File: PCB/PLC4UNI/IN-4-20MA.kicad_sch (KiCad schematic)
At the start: 8 parts

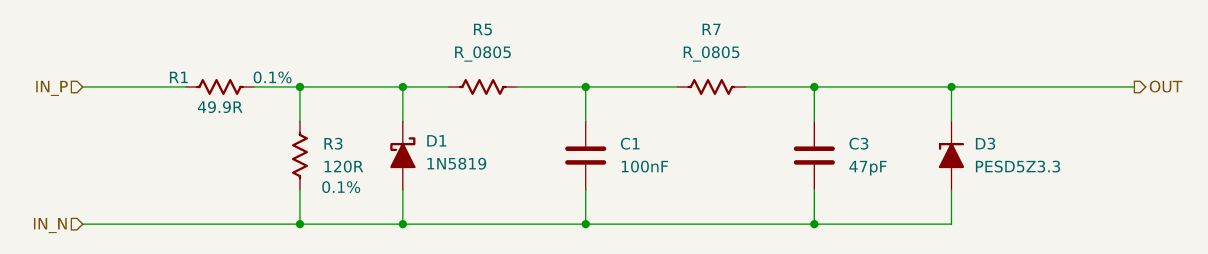
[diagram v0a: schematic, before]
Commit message: add ruteo buck-converter, inputs pnp,npn
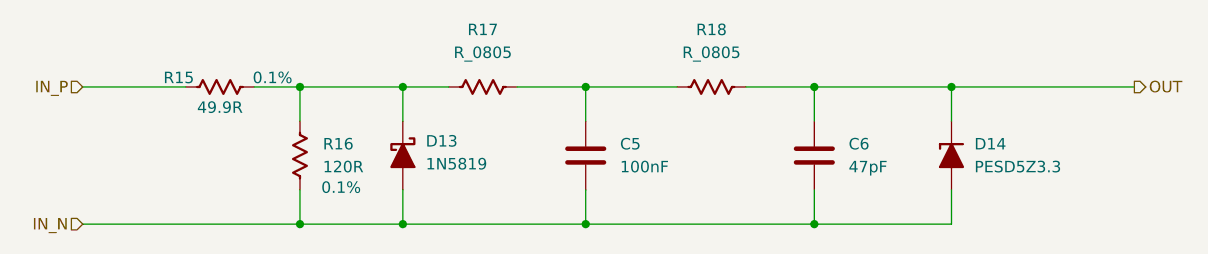
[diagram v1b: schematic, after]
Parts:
- renumbered C1 to C5, C3 to C6, D1 to D13, D3 to D14, R1 to R15, R3 to R16, R5 to R17, R7 to R18
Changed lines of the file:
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@@
 		(dnp no)
 		(fields_autoplaced yes)
-		(property "Reference" "R7"
+		(property "Reference" "R18"
 			(at 144.78 43.18 90)
 			(show_name no)
@@
 			(project "PLC4UNI"
 				(path "/f171b770-6a1a-4d3a-9dbb-25a622b94557/79ee6e1c-834c-43ff-8dcc-1385cc20b4c2/a71cebd4-7657-453a-a956-fcb918a861e5"
-					(reference "R7")
+					(reference "R18")
 					(unit 1)
 				)
 				(path "/f171b770-6a1a-4d3a-9dbb-25a622b94557/79ee6e1c-834c-43ff-8dcc-1385cc20b4c2/cfa02fc3-9ab3-4d43-96df-3d846bf37da2"
-					(reference "R8")
+					(reference "R22")
 					(unit 1)
 				)
@@
 		(in_pos_files yes)
 		(dnp no)
-		(property "Reference" "R3"
+		(property "Reference" "R16"
 			(at 101.6 55.8799 0)
 			(show_name no)
@@
 			(project "PLC4UNI"
 				(path "/f171b770-6a1a-4d3a-9dbb-25a622b94557/79ee6e1c-834c-43ff-8dcc-1385cc20b4c2/a71cebd4-7657-453a-a956-fcb918a861e5"
-					(reference "R3")
+					(reference "R16")
 					(unit 1)
 				)
 				(path "/f171b770-6a1a-4d3a-9dbb-25a622b94557/79ee6e1c-834c-43ff-8dcc-1385cc20b4c2/cfa02fc3-9ab3-4d43-96df-3d846bf37da2"
-					(reference "R4")
+					(reference "R20")
 					(unit 1)
 				)
@@
 		(dnp no)
 		(fields_autoplaced yes)
-		(property "Reference" "D1"
+		(property "Reference" "D13"
 			(at 113.03 55.5624 90)
 			(show_name no)
@@
 			(project "PLC4UNI"
 				(path "/f171b770-6a1a-4d3a-9dbb-25a622b94557/79ee6e1c-834c-43ff-8dcc-1385cc20b4c2/a71cebd4-7657-453a-a956-fcb918a861e5"
-					(reference "D1")
+					(reference "D13")
 					(unit 1)
 				)
 				(path "/f171b770-6a1a-4d3a-9dbb-25a622b94557/79ee6e1c-834c-43ff-8dcc-1385cc20b4c2/cfa02fc3-9ab3-4d43-96df-3d846bf37da2"
-					(reference "D2")
+					(reference "D15")
 					(unit 1)
 				)
@@
 		(dnp no)
 		(fields_autoplaced yes)
-		(property "Reference" "C3"
+		(property "Reference" "C6"
 			(at 160.02 55.8799 0)
 			(show_name no)
@@
 			(project "PLC4UNI"
 				(path "/f171b770-6a1a-4d3a-9dbb-25a622b94557/79ee6e1c-834c-43ff-8dcc-1385cc20b4c2/a71cebd4-7657-453a-a956-fcb918a861e5"
-					(reference "C3")
+					(reference "C6")
 					(unit 1)
 				)
 				(path "/f171b770-6a1a-4d3a-9dbb-25a622b94557/79ee6e1c-834c-43ff-8dcc-1385cc20b4c2/cfa02fc3-9ab3-4d43-96df-3d846bf37da2"
-					(reference "C4")
+					(reference "C8")
 					(unit 1)
 				)
@@
 		(dnp no)
 		(fields_autoplaced yes)
-		(property "Reference" "R5"
+		(property "Reference" "R17"
 			(at 119.38 43.18 90)
 			(show_name no)
@@
 			(project "PLC4UNI"
 				(path "/f171b770-6a1a-4d3a-9dbb-25a622b94557/79ee6e1c-834c-43ff-8dcc-1385cc20b4c2/a71cebd4-7657-453a-a956-fcb918a861e5"
-					(reference "R5")
+					(reference "R17")
 					(unit 1)
 				)
 				(path "/f171b770-6a1a-4d3a-9dbb-25a622b94557/79ee6e1c-834c-43ff-8dcc-1385cc20b4c2/cfa02fc3-9ab3-4d43-96df-3d846bf37da2"
-					(reference "R6")
+					(reference "R21")
 					(unit 1)
 				)
@@
 		(in_pos_files yes)
 		(dnp no)
-		(property "Reference" "R1"
+		(property "Reference" "R15"
 			(at 85.598 48.514 90)
 			(show_name no)
@@
 			(project "PLC4UNI"
 				(path "/f171b770-6a1a-4d3a-9dbb-25a622b94557/79ee6e1c-834c-43ff-8dcc-1385cc20b4c2/a71cebd4-7657-453a-a956-fcb918a861e5"
-					(reference "R1")
+					(reference "R15")
 					(unit 1)
 				)
 				(path "/f171b770-6a1a-4d3a-9dbb-25a622b94557/79ee6e1c-834c-43ff-8dcc-1385cc20b4c2/cfa02fc3-9ab3-4d43-96df-3d846bf37da2"
-					(reference "R2")
+					(reference "R19")
 					(unit 1)
 				)
@@
 		(dnp no)
 		(fields_autoplaced yes)
-		(property "Reference" "C1"
+		(property "Reference" "C5"
 			(at 134.62 55.8799 0)
 			(show_name no)
@@
 			(project "PLC4UNI"
 				(path "/f171b770-6a1a-4d3a-9dbb-25a622b94557/79ee6e1c-834c-43ff-8dcc-1385cc20b4c2/a71cebd4-7657-453a-a956-fcb918a861e5"
-					(reference "C1")
+					(reference "C5")
 					(unit 1)
 				)
 				(path "/f171b770-6a1a-4d3a-9dbb-25a622b94557/79ee6e1c-834c-43ff-8dcc-1385cc20b4c2/cfa02fc3-9ab3-4d43-96df-3d846bf37da2"
-					(reference "C2")
+					(reference "C7")
 					(unit 1)
 				)
@@
 		(dnp no)
 		(fields_autoplaced yes)
-		(property "Reference" "D3"
+		(property "Reference" "D14"
 			(at 173.99 55.8799 90)
 			(show_name no)
@@
 			(project "PLC4UNI"
 				(path "/f171b770-6a1a-4d3a-9dbb-25a622b94557/79ee6e1c-834c-43ff-8dcc-1385cc20b4c2/a71cebd4-7657-453a-a956-fcb918a861e5"
-					(reference "D3")
+					(reference "D14")
 					(unit 1)
 				)
 				(path "/f171b770-6a1a-4d3a-9dbb-25a622b94557/79ee6e1c-834c-43ff-8dcc-1385cc20b4c2/cfa02fc3-9ab3-4d43-96df-3d846bf37da2"
-					(reference "D4")
-					(unit 1)
-				)
+					(reference "D16")
+					(unit 1)
+				)

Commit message: 0-10V input, 4-20mA input
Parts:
- removed D13: 1N5819, PCM_Diode_THT_AKL:D_DO-41_SOD81_P7.62mm_Horizontal, symbol PCM_Diode_Schottky_AKL:1N5819
- added D13: 1N5819HW-7-F, EasyEDA:SOD-123_L2.7-W1.6-LS3.7-RD, symbol EasyEDA:1N5819HW-7-F
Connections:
- net IN_N: now also D13.2
- net at R15.2, R16.2, R17.1: now also D13.1
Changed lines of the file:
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@@
 	(wire
 		(pts
-			(xy 110.49 49.53) (xy 110.49 53.34)
+			(xy 110.49 49.53) (xy 110.49 52.07)
 		)
 		(stroke
@@
 	(wire
 		(pts
-			(xy 110.49 60.96) (xy 110.49 64.77)
-		)
-		(stroke
-			(width 0)
-			(type default)
-		)
-	)
-	(wire
-		(pts
 			(xy 123.19 49.53) (xy 130.81 49.53)
 		)
@@
 		(pts
 			(xy 171.45 49.53) (xy 171.45 53.34)
+		)
+		(stroke
+			(width 0)
+			(type default)
+		)
+	)
+	(wire
+		(pts
+			(xy 110.49 62.23) (xy 110.49 64.77)
 		)
 		(stroke
@@
 	)
 	(symbol
-		(lib_id "PCM_Diode_Schottky_AKL:1N5819")
-		(at 110.49 57.15 90)
-		(unit 1)
-		(body_style 1)
-		(exclude_from_sim no)
-		(in_bom yes)
-		(on_board yes)
-		(in_pos_files yes)
-		(dnp no)
-		(fields_autoplaced yes)
-		(property "Reference" "D13"
-			(at 113.03 55.5624 90)
-			(show_name no)
-			(do_not_autoplace no)
-			(effects
-				(font
-					(size 1.27 1.27)
-				)
-				(justify right)
-			)
-		)
-		(property "Value" "1N5819"
-			(at 113.03 58.1024 90)
-			(show_name no)
-			(do_not_autoplace no)
-			(effects
-				(font
-					(size 1.27 1.27)
-				)
-				(justify right)
-			)
-		)
-		(property "Footprint" "PCM_Diode_THT_AKL:D_DO-41_SOD81_P7.62mm_Horizontal"
-			(at 110.49 57.15 0)
-			(hide yes)
-			(show_name no)
-			(do_not_autoplace no)
-			(effects
-				(font
-					(size 1.27 1.27)
-				)
-			)
-		)
-		(property "Datasheet" "https://www.tme.eu/Document/1dcb17797cd83f32e896ece3030f14cc/1n5817-19.pdf"
-			(at 110.49 57.15 0)
-			(hide yes)
-			(show_name no)
-			(do_not_autoplace no)
-			(effects
-				(font
-					(size 1.27 1.27)
-				)
-			)
-		)
-		(property "Description" "DO-41 Schottky diode, 40V, 1A, Alternate KiCAD Library"
-			(at 110.49 57.15 0)
-			(hide yes)
-			(show_name no)
-			(do_not_autoplace no)
-			(effects
-				(font
-					(size 1.27 1.27)
-				)
-			)
-		)
-		(pin "2"
-		)
-		(pin "1"
-		)
-		(instances
-			(project "PLC4UNI"
-				(path "/f171b770-6a1a-4d3a-9dbb-25a622b94557/79ee6e1c-834c-43ff-8dcc-1385cc20b4c2/a71cebd4-7657-453a-a956-fcb918a861e5"
-					(reference "D13")
-					(unit 1)
-				)
-				(path "/f171b770-6a1a-4d3a-9dbb-25a622b94557/79ee6e1c-834c-43ff-8dcc-1385cc20b4c2/cfa02fc3-9ab3-4d43-96df-3d846bf37da2"
-					(reference "D15")
-					(unit 1)
-				)
-			)
-		)
-	)
-	(symbol
 		(lib_id "PCM_Capacitor_US_AKL:C_0603")
 		(at 156.21 57.15 0)
@@
 					(unit 1)
 				)
+			)
+		)
+	)
+	(symbol
+		(lib_id "EasyEDA:1N5819HW-7-F")
+		(at 110.49 57.15 270)
+		(unit 1)
+		(body_style 1)
+		(exclude_from_sim no)
+		(in_bom yes)
+		(on_board yes)
+		(in_pos_files yes)
+		(dnp no)
+		(fields_autoplaced yes)
+		(property "Reference" "D13"
+			(at 114.3 55.4999 90)
+			(show_name no)
+			(do_not_autoplace no)
+			(effects
+				(font
+					(size 1.27 1.27)
+				)
+				(justify left)
+			)
+		)
+		(property "Value" "1N5819HW-7-F"
+			(at 114.3 58.0399 90)
+			(show_name no)
+			(do_not_autoplace no)
+			(effects
+				(font
+					(size 1.27 1.27)
+				)
+				(justify left)
+			)
+		)
+		(property "Footprint" "EasyEDA:SOD-123_L2.7-W1.6-LS3.7-RD"
+			(at 102.87 57.15 0)
+			(hide yes)
+			(show_name no)
+			(do_not_autoplace no)
+			(effects
+				(font
+					(size 1.27 1.27)
+				)
+			)
+		)
+		(property "Datasheet" "https://lcsc.com/product-detail/Schottky-Barrier-Diodes-SBD_DIODES_1N5819HW-7-F_1N5819HW-7-F_C82544.html"
+			(at 100.33 57.15 0)
+			(hide yes)
+			(show_name no)
+			(do_not_autoplace no)
+			(effects
+				(font
+					(size 1.27 1.27)
+				)
+			)
+		)
+		(property "Description" "1N5819HW-7-F"
+			(at 87.63 57.15 0)
+			(hide yes)
+			(show_name no)
+			(do_not_autoplace no)
+			(effects
+				(font
+					(size 1.27 1.27)
+				)
+			)
+		)
+		(property "Manufacturer" "DIODES(美台)"
+			(at 97.79 57.15 0)
+			(hide yes)
+			(show_name no)
+			(do_not_autoplace no)
+			(effects
+				(font
+					(size 1.27 1.27)
+				)
+			)
+		)
+		(property "MPN" "1N5819HW-7-F"
+			(at 95.25 57.15 0)
+			(hide yes)
+			(show_name no)
+			(do_not_autoplace no)
+			(effects
+				(font
+					(size 1.27 1.27)
+				)
+			)
+		)
+		(property "LCSC Part" "C82544"
+			(at 92.71 57.15 0)
+			(hide yes)
+			(show_name no)
+			(do_not_autoplace no)
+			(effects
+				(font
+					(size 1.27 1.27)
+				)
+			)
+		)
+		(pin "2"
+		)
+		(pin "1"
+		)
+		(instances
+			(project "PLC4UNI"
+				(path "/f171b770-6a1a-4d3a-9dbb-25a622b94557/79ee6e1c-834c-43ff-8dcc-1385cc20b4c2/a71cebd4-7657-453a-a956-fcb918a861e5"
+					(reference "D13")
+					(unit 1)
+				)
+				(path "/f171b770-6a1a-4d3a-9dbb-25a622b94557/79ee6e1c-834c-43ff-8dcc-1385cc20b4c2/cfa02fc3-9ab3-4d43-96df-3d846bf37da2"
+					(reference "D15")
+					(unit 1)
+				)

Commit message: power supply and inputs routed
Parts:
- C5: footprint PCM_Capacitor_SMD_AKL:C_0603_1608Metric -> TestPoint:TestPoint_THTPad_D1.5mm_Drill0.7mm
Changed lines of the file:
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@@
 			)
 		)
-		(property "Footprint" "PCM_Capacitor_SMD_AKL:C_0603_1608Metric"
+		(property "Footprint" "TestPoint:TestPoint_THTPad_D1.5mm_Drill0.7mm"
 			(at 131.7752 60.96 0)
 			(hide yes)
